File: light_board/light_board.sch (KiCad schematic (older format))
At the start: 17 parts, among them J1 CONN_01X02, J2 Led_Connector, J3 Power_Connector, Q1 FDC658AP, U1 LM3409MY

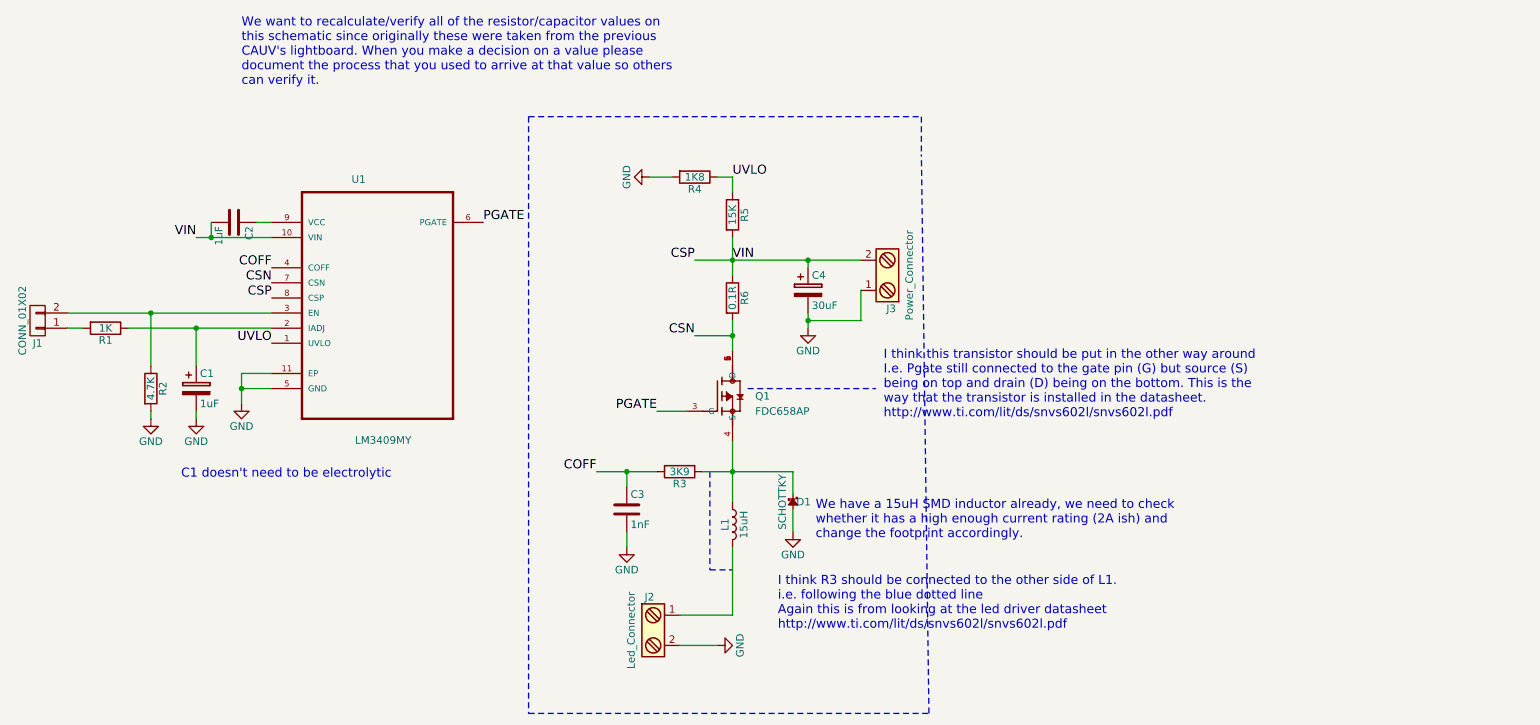
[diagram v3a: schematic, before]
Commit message: changed orientation of pmos and the wiring of R3
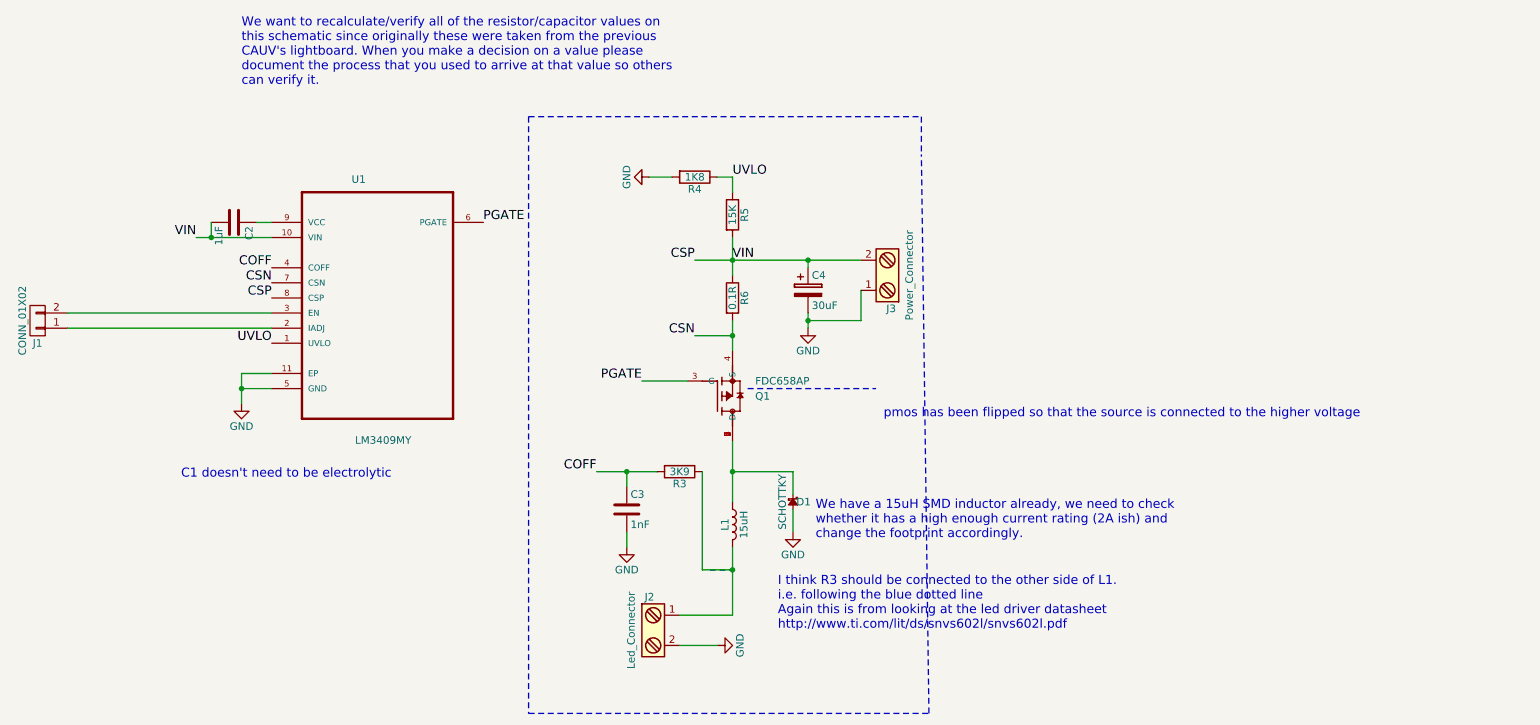
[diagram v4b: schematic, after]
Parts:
- removed C1: 1uF, Capacitors_THT:CP_Radial_Tantal_D5.0mm_P2.50mm, symbol CP
- removed R1: 1K, Resistors_SMD:R_0603, symbol R
- removed R2: 4.7K, Resistors_SMD:R_0603, symbol R
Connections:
- net CSN: now also Q1.4 (S); no longer Q1.1 (D), Q1.2 (D), Q1.5 (D), Q1.6 (D)
- net at U1.2 (IADJ): now also J1.1 (P1)
- net at D1.1, L1.1: now also Q1.1 (D), Q1.2 (D), Q1.5 (D), Q1.6 (D); no longer Q1.4 (S), R3.1
- net at J2.1, L1.2: now also R3.1
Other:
- note added: "pmos has been flipped so that the source is connected to the higher voltage"
- note removed: "I think this transistor should be put in the other way around\nI.e. Pgate still connected to the gate pin (G) but source (S) \nbeing on top and drain (D) being on the bottom. This is the\nway that the transistor is installed in the datasheet. \nhttp://www.ti.com/lit/ds/snvs602l/snvs602l.pdf"
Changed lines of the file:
@@
 UVLO
-$Comp
-L R R1
-U 1 1 58D53FEE
-P 4100 3500
-F 0 "R1" V 4180 3500 50  0000 C CNN
-F 1 "1K" V 4100 3500 50  0000 C CNN
-F 2 "Resistors_SMD:R_0603" V 4030 3500 50  0001 C CNN
-F 3 "" H 4100 3500 50  0001 C CNN
-	1    4100 3500
-	0    1    1    0
-$EndComp
-$Comp
-L GND #PWR02
-U 1 1 58D54081
-P 4400 4100
-F 0 "#PWR02" H 4400 3850 50  0001 C CNN
-F 1 "GND" H 4400 3950 50  0000 C CNN
-F 2 "" H 4400 4100 50  0001 C CNN
-F 3 "" H 4400 4100 50  0001 C CNN
-	1    4400 4100
-	1    0    0    -1
-$EndComp
-$Comp
-L GND #PWR03
-U 1 1 58D540A1
-P 4700 4100
-F 0 "#PWR03" H 4700 3850 50  0001 C CNN
-F 1 "GND" H 4700 3950 50  0000 C CNN
-F 2 "" H 4700 4100 50  0001 C CNN
-F 3 "" H 4700 4100 50  0001 C CNN
-	1    4700 4100
-	1    0    0    -1
-$EndComp
 $Comp
 L CONN_01X02 J1
@@
 Text Label 7350 4450 2    60   ~ 0
 COFF
-Text Label 7750 4050 2    60   ~ 0
+Text Label 7650 3850 2    60   ~ 0
 PGATE
 Text Label 8000 3550 2    60   ~ 0
@@
 $EndComp
 $Comp
-L CP C1
-U 1 1 58D5656D
-P 4700 3900
-F 0 "C1" H 4725 4000 50  0000 L CNN
-F 1 "1uF" H 4725 3800 50  0000 L CNN
-F 2 "Capacitors_THT:CP_Radial_Tantal_D5.0mm_P2.50mm" H 4738 3750 50  0001 C CNN
-F 3 "" H 4700 3900 50  0001 C CNN
-	1    4700 3900
-	1    0    0    -1
-$EndComp
-$Comp
 L Screw_Terminal_1x02 J2
 U 1 1 58D56F37
@@
 F 3 "" H 7675 5500 50  0001 C CNN
 	1    7700 5500
-	1    0    0    -1
-$EndComp
-$Comp
-L R R2
-U 1 1 58D53F94
-P 4400 3900
-F 0 "R2" V 4480 3900 50  0000 C CNN
-F 1 "4.7K" V 4400 3900 50  0000 C CNN
-F 2 "Resistors_SMD:R_0603" V 4330 3900 50  0001 C CNN
-F 3 "" H 4400 3900 50  0001 C CNN
-	1    4400 3900
 	1    0    0    -1
 $EndComp
@@
 F 8 "TSOT-23-6 Fairchild Semiconductor" H 8150 3950 50  0001 L CNN "Package"
 	1    8150 3950
-	1    0    0    -1
+	1    0    0    1
 $EndComp
 $Comp
@@
 	-1   0    0    1
 $EndComp
-Text Notes 9250 4100 0    60   ~ 0
-I think this transistor should be put in the other way around\nI.e. Pgate still connected to the gate pin (G) but source (S) \nbeing on top and drain (D) being on the bottom. This is the\nway that the transistor is installed in the datasheet. \nhttp://www.ti.com/lit/ds/snvs602l/snvs602l.pdf
 Wire Wire Line
 	5200 3800 5000 3800
@@
 Connection ~ 5000 3900
 Wire Wire Line
-	5200 3500 4250 3500
-Wire Wire Line
-	4700 3750 4700 3500
-Connection ~ 4700 3500
-Wire Wire Line
-	4400 3750 4400 3400
+	3850 3500 5200 3500
 Wire Wire Line
 	3850 3400 5200 3400
-Wire Wire Line
-	3850 3500 3950 3500
-Connection ~ 4400 3400
 Wire Wire Line
 	5100 2800 5200 2800
@@
 	8250 2500 8250 2600
 Wire Wire Line
-	8050 4450 8650 4450
+	8250 4450 8650 4450
 Wire Wire Line
 	8250 4250 8250 4650
@@
 	8250 4950 8250 5400
 Wire Wire Line
-	8250 3650 8250 3450
+	8250 3450 8250 3650
 Wire Wire Line
 	8000 3550 8250 3550
@@
 	8250 5400 7900 5400
 Wire Wire Line
-	4400 4050 4400 4100
-Wire Wire Line
-	4700 4100 4700 4050
-Wire Wire Line
 	7900 5600 8150 5600
 Wire Wire Line
-	7950 4050 7750 4050
-Wire Wire Line
-	8750 3500 8750 3400
+	7950 3850 7650 3850
+Wire Wire Line
+	8750 3400 8750 3500
 Wire Notes Line
 	6900 2100 6900 6050
@@
 Text Notes 8550 5500 0    60   ~ 0
 I think R3 should be connected to the other side of L1.\ni.e. following the blue dotted line\nAgain this is from looking at the led driver datasheet\nhttp://www.ti.com/lit/ds/snvs602l/snvs602l.pdf
-Wire Notes Line
-	8100 4450 8100 5100
 Wire Notes Line
 	8100 5100 8250 5100
@@
 Text Notes 4600 4500 0    60   ~ 0
 C1 doesn't need to be electrolytic
+Wire Wire Line
+	8050 4450 8050 5100
+Wire Wire Line
+	8050 5100 8250 5100
+Connection ~ 8250 5100
+Text Notes 9250 4100 0    60   ~ 0
+pmos has been flipped so that the source is connected to the higher voltage
 $EndSCHEMATC

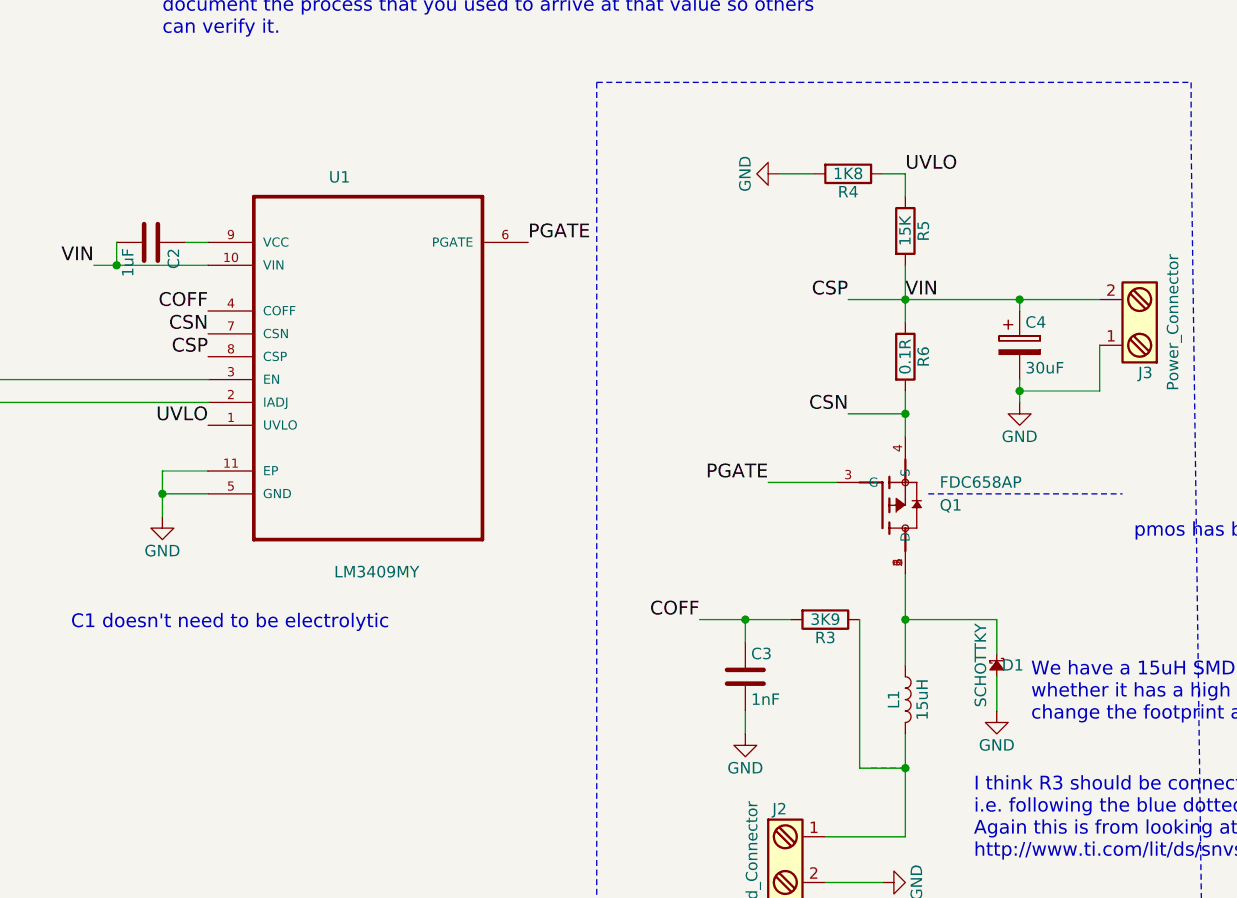
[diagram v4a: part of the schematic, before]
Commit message: changed values and names in eeschema file
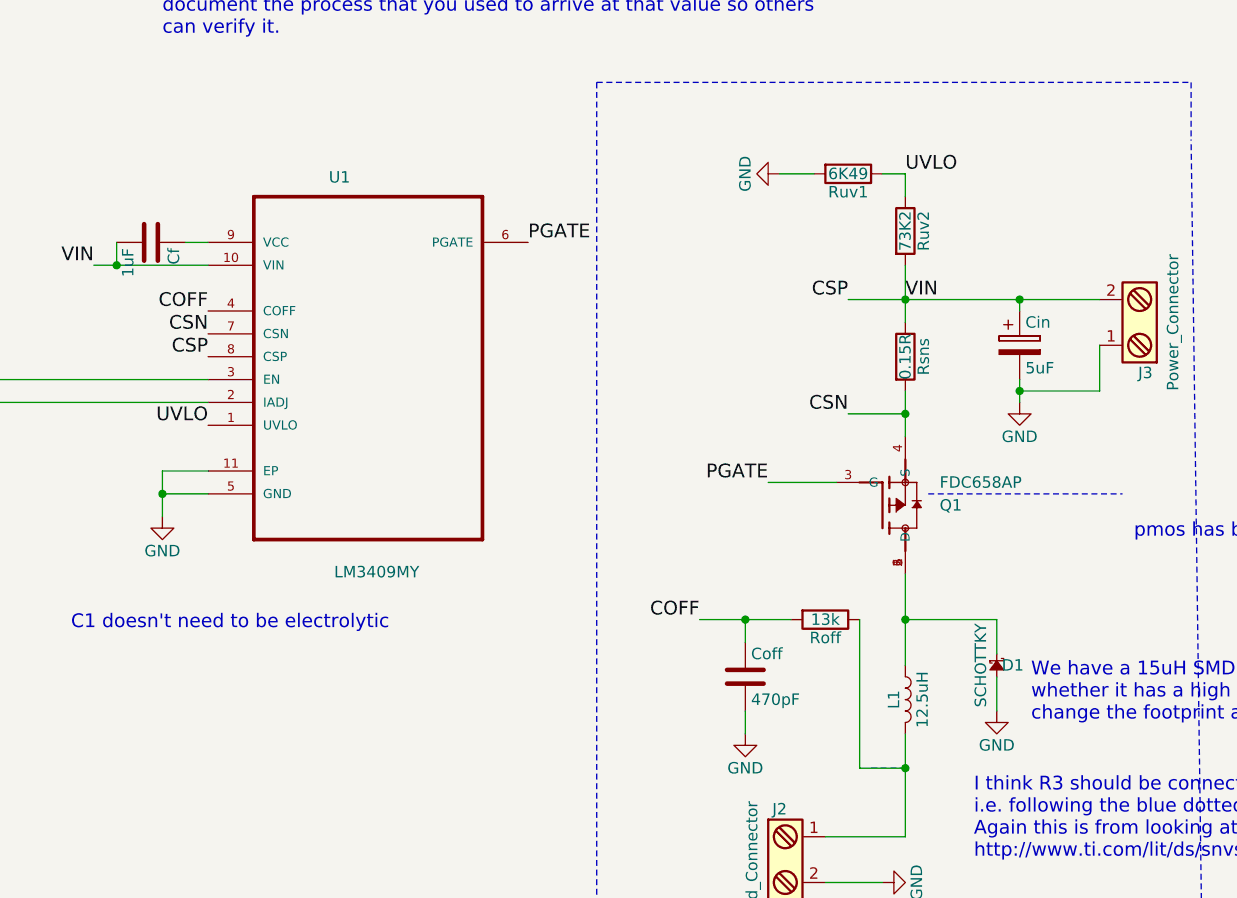
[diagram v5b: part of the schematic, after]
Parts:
- Cin: renamed from C4; value 30uF -> 5uF
- Coff: renamed from C3; value 1nF -> 470pF
- L1: value 15uH -> 12.5uH
- Roff: renamed from R3; value 3K9 -> 13k
- Rsns: renamed from R6; value 0.1R -> 0.15R
- Ruv1: renamed from R4; value 1K8 -> 6K49
- Ruv2: renamed from R5; value 15K -> 73K2
- renumbered C2 to Cf
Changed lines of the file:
@@
 $EndComp
 $Comp
-L C C2
+L C Cf
 U 1 1 58D54246
 P 4950 2800
-F 0 "C2" H 4975 2900 50  0000 L CNN
+F 0 "Cf" H 4975 2900 50  0000 L CNN
 F 1 "1uF" H 4975 2700 50  0000 L CNN
 F 2 "Capacitors_SMD:C_0603" H 4988 2650 50  0001 C CNN
@@
 UVLO
 $Comp
-L R R4
+L R Ruv1
 U 1 1 58D54C6B
 P 8000 2500
-F 0 "R4" V 8080 2500 50  0000 C CNN
-F 1 "1K8" V 8000 2500 50  0000 C CNN
+F 0 "Ruv1" V 8080 2500 50  0000 C CNN
+F 1 "6K49" V 8000 2500 50  0000 C CNN
 F 2 "Resistors_SMD:R_0603" V 7930 2500 50  0001 C CNN
 F 3 "" H 8000 2500 50  0001 C CNN
@@
 $EndComp
 $Comp
-L R R5
+L R Ruv2
 U 1 1 58D54CCF
 P 8250 2750
-F 0 "R5" V 8330 2750 50  0000 C CNN
-F 1 "15K" V 8250 2750 50  0000 C CNN
+F 0 "Ruv2" V 8330 2750 50  0000 C CNN
+F 1 "73K2" V 8250 2750 50  0000 C CNN
 F 2 "Resistors_SMD:R_0603" V 8180 2750 50  0001 C CNN
 F 3 "" H 8250 2750 50  0001 C CNN
@@
 CSP
 $Comp
-L C C3
+L C Coff
 U 1 1 58D550FA
 P 7550 4700
-F 0 "C3" H 7575 4800 50  0000 L CNN
-F 1 "1nF" H 7575 4600 50  0000 L CNN
+F 0 "Coff" H 7575 4800 50  0000 L CNN
+F 1 "470pF" H 7575 4600 50  0000 L CNN
 F 2 "Capacitors_SMD:C_0603" H 7588 4550 50  0001 C CNN
 F 3 "" H 7550 4700 50  0001 C CNN
@@
 $EndComp
 $Comp
-L R R3
+L R Roff
 U 1 1 58D55135
 P 7900 4450
-F 0 "R3" V 7980 4450 50  0000 C CNN
-F 1 "3K9" V 7900 4450 50  0000 C CNN
+F 0 "Roff" V 7980 4450 50  0000 C CNN
+F 1 "13k" V 7900 4450 50  0000 C CNN
 F 2 "Resistors_SMD:R_0603" V 7830 4450 50  0001 C CNN
 F 3 "" H 7900 4450 50  0001 C CNN
@@
 P 8250 4800
 F 0 "L1" V 8200 4800 50  0000 C CNN
-F 1 "15uH" V 8325 4800 50  0000 C CNN
+F 1 "12.5uH" V 8325 4800 50  0000 C CNN
 F 2 "Inductors_THT:L_Axial_L16.0mm_D6.3mm_P25.40mm_Horizontal_Fastron_VHBCC" H 8250 4800 50  0001 C CNN
 F 3 "" H 8250 4800 50  0001 C CNN
@@
 $EndComp
 $Comp
-L R R6
+L R Rsns
 U 1 1 58D55809
 P 8250 3300
-F 0 "R6" V 8330 3300 50  0000 C CNN
-F 1 "0.1R" V 8250 3300 50  0000 C CNN
+F 0 "Rsns" V 8330 3300 50  0000 C CNN
+F 1 "0.15R" V 8250 3300 50  0000 C CNN
 F 2 "Resistors_THT:R_Axial_DIN0614_L14.3mm_D5.7mm_P15.24mm_Horizontal" V 8180 3300 50  0001 C CNN
 F 3 "" H 8250 3300 50  0001 C CNN
@@
 $EndComp
 $Comp
-L CP C4
+L CP Cin
 U 1 1 58D559B3
 P 8750 3250
-F 0 "C4" H 8775 3350 50  0000 L CNN
-F 1 "30uF" H 8775 3150 50  0000 L CNN
+F 0 "Cin" H 8775 3350 50  0000 L CNN
+F 1 "5uF" H 8775 3150 50  0000 L CNN
 F 2 "Capacitors_THT:CP_Radial_Tantal_D5.0mm_P2.50mm" H 8788 3100 50  0001 C CNN
 F 3 "" H 8750 3250 50  0001 C CNN
